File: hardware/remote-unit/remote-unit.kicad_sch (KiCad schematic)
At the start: 54 parts, among them J1 SOL_A, J2 RF Module, J3 ICSP, J4 IO, J5 SOL_B, J6 PWR 12V, J7 UART, J8 I2C, J9 SOLAR, Q1 N >1A@4VGS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

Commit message: Update irrigation controller board
Remove atmega328p
Remove 5v voltage regulator
Replace max485 with max3485
Remove signal relays
Add female headers for ESP32
Add two LEDs
Update BOM based on JLCPCB availability
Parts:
- L1: JLCPCB Part C253606 -> C497847
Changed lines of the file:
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@@
       (effects (font (size 1.27 1.27)) hide)
     )
-    (property "JLCPCB Part" "C253606" (at 184.15 24.13 0)
+    (property "JLCPCB Part" "C497847" (at 184.15 24.13 0)
       (effects (font (size 1.27 1.27)) hide)
     )

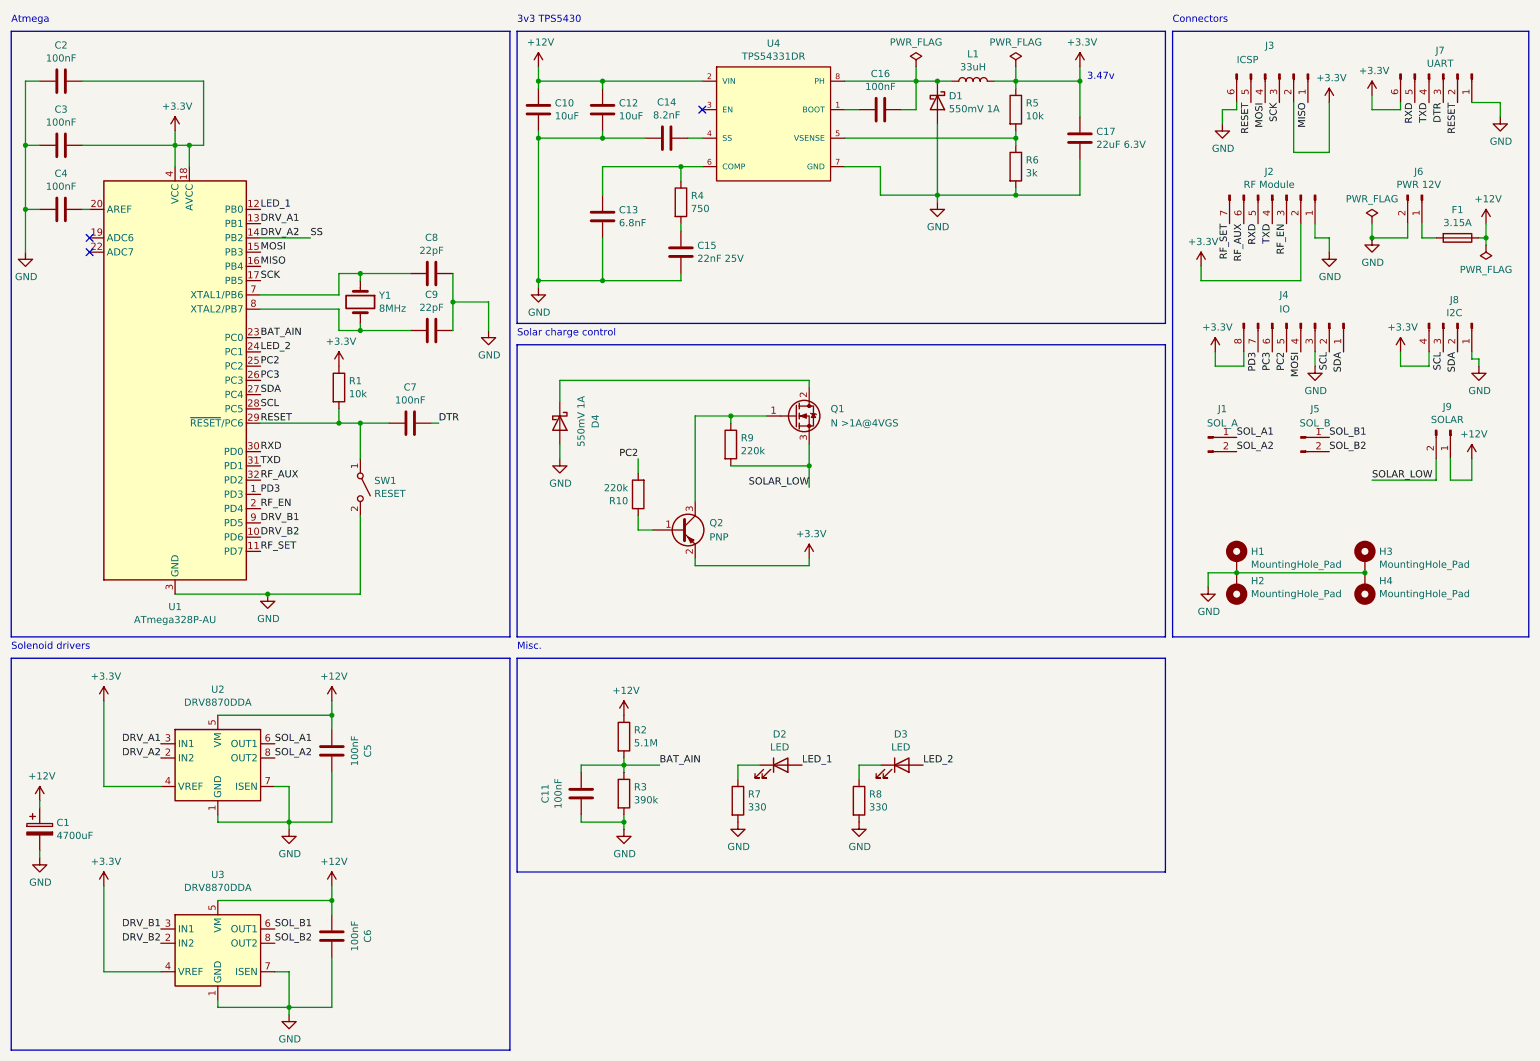
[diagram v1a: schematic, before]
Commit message: Add RS485 to remote unit schematic
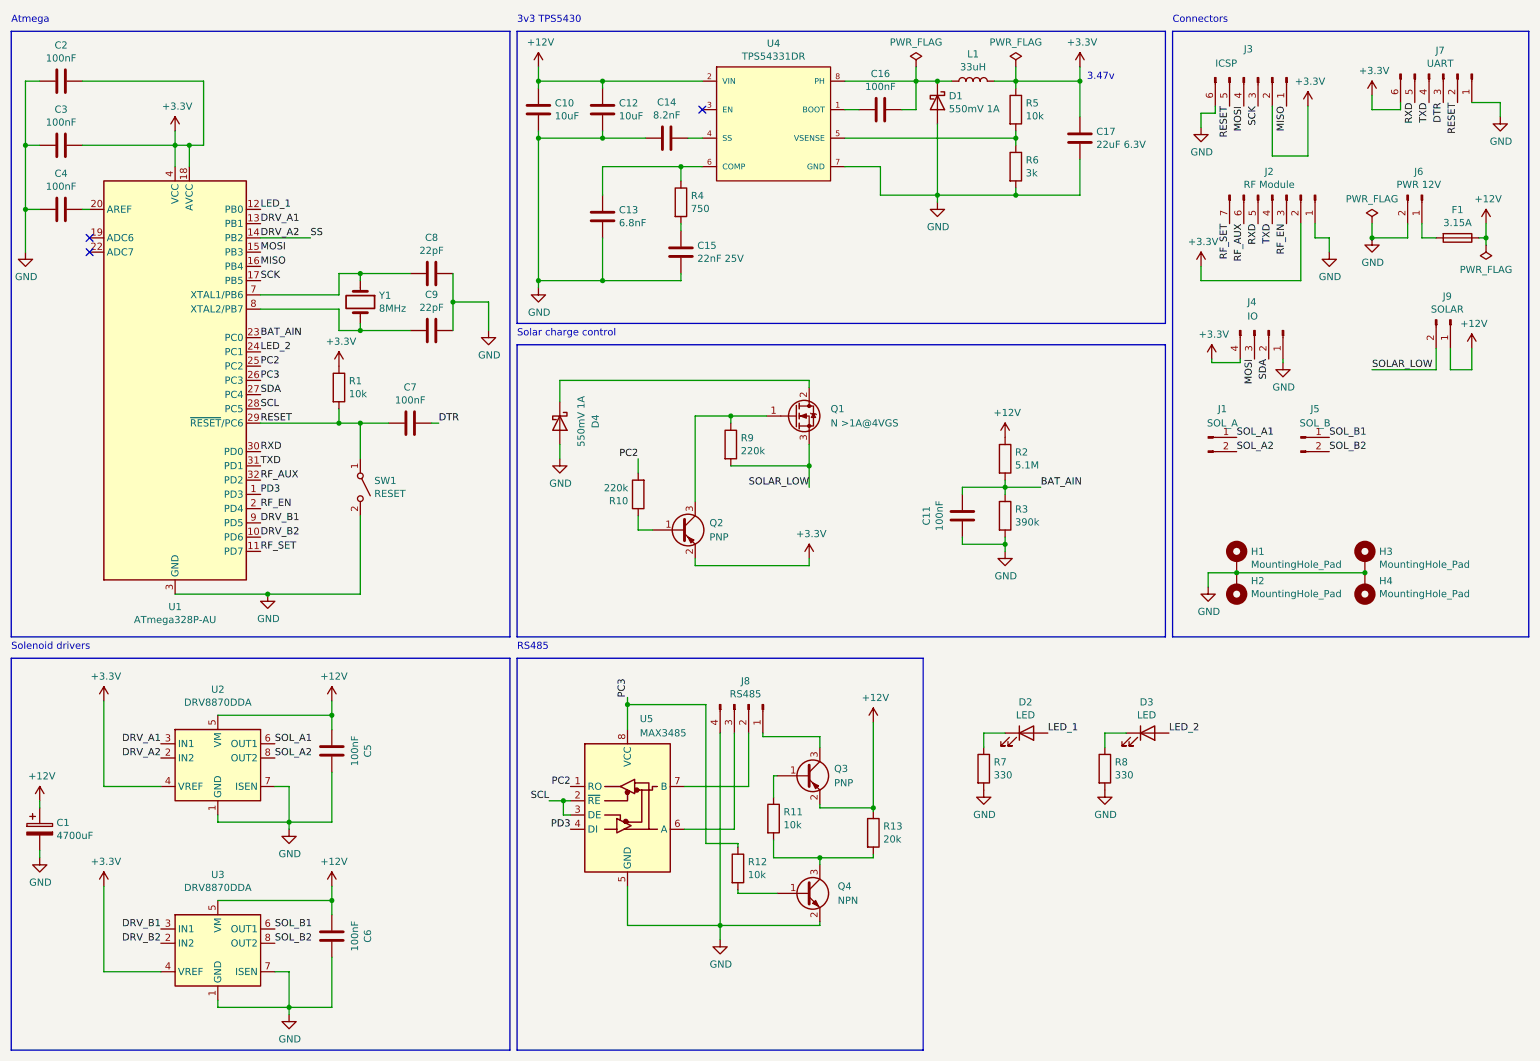
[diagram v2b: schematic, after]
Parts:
- added Q3: PNP, Package_TO_SOT_SMD:SOT-23, symbol Device:Q_PNP_BEC
- added Q4: NPN, Package_TO_SOT_SMD:SOT-23, symbol Device:Q_NPN_BEC
- added R11, R12: 10k, Resistor_SMD:R_0402_1005Metric, symbol Device:R
- added R13: 20k, Resistor_SMD:R_0402_1005Metric, symbol Device:R
- added U5: MAX3485, Package_DIP:DIP-8_W7.62mm, symbol Interface_UART:MAX3485
- C1: symbol remote-unit-rescue:CP-Device -> Device:C_Polarized
- J1, J5, J6, J9: symbol remote-unit-rescue:Conn_01x02_Male-Connector -> Connector:Conn_01x02_Pin
- J2: symbol remote-unit-rescue:Conn_01x07_Male-Connector -> Connector:Conn_01x07_Pin
- J3, J7: symbol remote-unit-rescue:Conn_01x06_Male-Connector -> Connector:Conn_01x06_Pin
- J4: symbol remote-unit-rescue:Conn_01x08_Male-Connector -> Connector:Conn_01x04_Pin
- J8: value I2C -> RS485
- U1: symbol remote-unit-rescue:ATmega328P-AU-MCU_Microchip_ATmega -> MCU_Microchip_ATmega:ATmega328P-A
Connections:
- net +12V: now also Q3.2 (E), R13.1
- net +3.3V: now also J4.4 (Pin_4); no longer J4.8 (Pin_8), J8.4 (Pin_4)
- net GND: now also J4.1 (Pin_1), J8.4 (Pin_4), Q4.2 (E), U5.5 (GND); no longer J4.3 (Pin_3), J8.1 (Pin_1)
- net MOSI: now also J4.3 (Pin_3); no longer J4.4 (Pin_4)
- net PC2: now also U5.1 (RO); no longer J4.5 (Pin_5)
- net PC3: now also R12.1, U5.8 (VCC); no longer J4.6 (Pin_6)
- net PD3: now also U5.4 (DI); no longer J4.7 (Pin_7)
- net SCL: now also U5.2 (~{RE}), U5.3 (DE); no longer J4.2 (Pin_2), J8.3 (Pin_3)
- net SDA: now also J4.2 (Pin_2); no longer J4.1 (Pin_1), J8.2 (Pin_2)
- new net: J8.1 (Pin_1), Q3.3 (C)
- new net: J8.2 (Pin_2), U5.7 (B)
- new net: J8.3 (Pin_3), U5.6 (A)
- new net: Q4.1 (B), R12.2
- new net: Q4.3 (C), R11.2, R13.2
- new net: Q3.1 (B), R11.1
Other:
- note added: "RS485"
- note removed: "Misc."
- moved on the sheet: C11, D2, D3, J3, J8, J9, R2, R3, R7, R8

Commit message: Update remote unit PCB
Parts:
- removed J4: IO, Connector_PinHeader_2.54mm:PinHeader_2x04_P2.54mm_Vertical, symbol Connector:Conn_01x04_Pin
- D2, D3: footprint LED_SMD:LED_0603_1608Metric_Castellated -> LED_SMD:LED_0603_1608Metric
- H1, H2, H3, H4: now left out of the parts list
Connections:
- net PC2: no longer R10.2
- net SCL renamed PC5
- net SDA renamed PC4
- net PC4: now also R10.2
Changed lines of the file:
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@@
-    (stroke (width 0) (type default))
-  )
-  (wire (pts (xy 239.395 73.66) (xy 239.395 74.295))
     (stroke (width 0) (type default))
   )
@@
     (stroke (width 0) (type default))
   )
-  (wire (pts (xy 231.775 73.66) (xy 231.775 74.295))
-    (stroke (width 0) (type default))
-  )
   (wire (pts (xy 243.84 37.465) (xy 243.84 28.575))
     (stroke (width 0) (type default))
@@
     (stroke (width 0) (type default))
   )
-  (wire (pts (xy 226.695 74.295) (xy 226.695 73.66))
-    (stroke (width 0) (type default))
-  )
   (wire (pts (xy 189.865 96.52) (xy 189.865 97.79))
     (stroke (width 0) (type default))
@@
     (stroke (width 0) (type default))
   )
-  (wire (pts (xy 231.775 74.295) (xy 226.695 74.295))
-    (stroke (width 0) (type default))
-  )
   (wire (pts (xy 154.94 77.47) (xy 154.94 78.74))
     (stroke (width 0) (type default))
@@
   (label "LED_2" (at 57.15 72.39 0) (fields_autoplaced)
     (effects (font (size 1.27 1.27)) (justify left bottom))
-  )
-  (label "MOSI" (at 234.315 73.66 270) (fields_autoplaced)
-    (effects (font (size 1.27 1.27)) (justify right bottom))
   )
   (label "RXD" (at 234.95 49.53 270) (fields_autoplaced)
@@
     (effects (font (size 1.27 1.27)) (justify left bottom))
   )
-  (label "SDA" (at 57.15 80.01 0) (fields_autoplaced)
+  (label "PC4" (at 57.15 80.01 0) (fields_autoplaced)
     (effects (font (size 1.27 1.27)) (justify left bottom))
   )
@@
     (effects (font (size 1.27 1.27)) (justify left bottom))
   )
-  (label "SCL" (at 108.585 152.4 180) (fields_autoplaced)
+  (label "PC5" (at 108.585 152.4 180) (fields_autoplaced)
     (effects (font (size 1.27 1.27)) (justify right bottom))
   )
@@
     (effects (font (size 1.27 1.27)) (justify right bottom))
   )
-  (label "SDA" (at 236.855 73.66 270) (fields_autoplaced)
-    (effects (font (size 1.27 1.27)) (justify right bottom))
-  )
   (label "MISO" (at 240.03 28.575 270) (fields_autoplaced)
     (effects (font (size 1.27 1.27)) (justify right bottom))
@@
     (effects (font (size 1.27 1.27)) (justify left bottom))
   )
-  (label "PC2" (at 124.46 91.44 180) (fields_autoplaced)
+  (label "PC4" (at 124.46 91.44 180) (fields_autoplaced)
     (effects (font (size 1.27 1.27)) (justify right bottom))
   )
@@
     (effects (font (size 1.27 1.27)) (justify left bottom))
   )
-  (label "SCL" (at 57.15 82.55 0) (fields_autoplaced)
+  (label "PC5" (at 57.15 82.55 0) (fields_autoplaced)
     (effects (font (size 1.27 1.27)) (justify left bottom))
   )
@@
       (effects (font (size 1.27 1.27)))
     )
-    (property "Footprint" "LED_SMD:LED_0603_1608Metric_Castellated" (at 193.675 140.335 0)
+    (property "Footprint" "LED_SMD:LED_0603_1608Metric" (at 193.675 140.335 0)
       (effects (font (size 1.27 1.27)) hide)
     )
@@
       (effects (font (size 1.27 1.27)))
     )
-    (property "Footprint" "LED_SMD:LED_0603_1608Metric_Castellated" (at 215.265 140.335 0)
+    (property "Footprint" "LED_SMD:LED_0603_1608Metric" (at 215.265 140.335 0)
       (effects (font (size 1.27 1.27)) hide)
     )
@@
     )
   )
-  (symbol (lib_id "Connector:Conn_01x04_Pin") (at 236.855 68.58 270) (unit 1)
-    (in_bom yes) (on_board yes) (dnp no)
-    (property "Reference" "J4" (at 233.045 63.5 90)
-      (effects (font (size 1.27 1.27)) (justify left))
-    )
-    (property "Value" "IO" (at 233.045 66.04 90)
-      (effects (font (size 1.27 1.27)) (justify left))
-    )
-    (property "Footprint" "Connector_PinHeader_2.54mm:PinHeader_2x04_P2.54mm_Vertical" (at 236.855 68.58 0)
-      (effects (font (size 1.27 1.27)) hide)
-    )
-    (property "Datasheet" "~" (at 236.855 68.58 0)
-      (effects (font (size 1.27 1.27)) hide)
-    )
-    (property "Purchase Link" "https://au.element14.com/amphenol-icc/77313-801-20lf/conn-header-20pos-2row-2-54mm/dp/3728842" (at 236.855 68.58 0)
-      (effects (font (size 1.27 1.27)) hide)
-    )
-    (pin "1")
-    (pin "2")
-    (pin "3")
-    (pin "4")
-    (instances
-      (project "remote-unit"
-        (path "/18be3b1b-9bcf-4c4f-bb2a-ca2504ea30e0"
-          (reference "J4") (unit 1)
-        )
-      )
-    )
-  )
-  (symbol (lib_id "power:+3.3V") (at 226.695 73.66 0) (unit 1)
-    (in_bom yes) (on_board yes) (dnp no)
-    (property "Reference" "#PWR022" (at 226.695 77.47 0)
-      (effects (font (size 1.27 1.27)) hide)
-    )
-    (property "Value" "+3.3V" (at 227.076 69.2658 0)
-      (effects (font (size 1.27 1.27)))
-    )
-    (property "Footprint" "" (at 226.695 73.66 0)
-      (effects (font (size 1.27 1.27)) hide)
-    )
-    (property "Datasheet" "" (at 226.695 73.66 0)
-      (effects (font (size 1.27 1.27)) hide)
-    )
-    (pin "1")
-    (instances
-      (project "remote-unit"
-        (path "/18be3b1b-9bcf-4c4f-bb2a-ca2504ea30e0"
-          (reference "#PWR022") (unit 1)
-        )
-      )
-    )
-  )
-  (symbol (lib_id "power:GND") (at 239.395 74.295 0) (unit 1)
-    (in_bom yes) (on_board yes) (dnp no)
-    (property "Reference" "#PWR026" (at 239.395 80.645 0)
-      (effects (font (size 1.27 1.27)) hide)
-    )
-    (property "Value" "GND" (at 239.522 78.6892 0)
-      (effects (font (size 1.27 1.27)))
-    )
-    (property "Footprint" "" (at 239.395 74.295 0)
-      (effects (font (size 1.27 1.27)) hide)
-    )
-    (property "Datasheet" "" (at 239.395 74.295 0)
-      (effects (font (size 1.27 1.27)) hide)
-    )
-    (pin "1")
-    (instances
-      (project "remote-unit"
-        (path "/18be3b1b-9bcf-4c4f-bb2a-ca2504ea30e0"
-          (reference "#PWR026") (unit 1)
-        )
-      )
-    )
-  )
   (symbol (lib_id "power:+3.3V") (at 29.21 134.62 0) (unit 1)
     (in_bom yes) (on_board yes) (dnp no)
@@
   )
   (symbol (lib_id "Mechanical:MountingHole_Pad") (at 231.14 109.22 0) (unit 1)
-    (in_bom yes) (on_board yes) (dnp no)
+    (in_bom no) (on_board yes) (dnp no)
     (property "Reference" "H1" (at 233.68 107.9754 0)
       (effects (font (size 1.27 1.27)) (justify left))
@@
   )
   (symbol (lib_id "Mechanical:MountingHole_Pad") (at 254 109.22 0) (unit 1)
-    (in_bom yes) (on_board yes) (dnp no)
+    (in_bom no) (on_board yes) (dnp no)
     (property "Reference" "H3" (at 256.54 107.9754 0)
       (effects (font (size 1.27 1.27)) (justify left))
@@
   )
   (symbol (lib_id "Mechanical:MountingHole_Pad") (at 231.14 114.3 180) (unit 1)
-    (in_bom yes) (on_board yes) (dnp no)
+    (in_bom no) (on_board yes) (dnp no)
     (property "Reference" "H2" (at 233.68 113.2078 0)
       (effects (font (size 1.27 1.27)) (justify right))
@@
   )
   (symbol (lib_id "Mechanical:MountingHole_Pad") (at 254 114.3 180) (unit 1)
-    (in_bom yes) (on_board yes) (dnp no)
+    (in_bom no) (on_board yes) (dnp no)
     (property "Reference" "H4" (at 256.54 113.2078 0)
       (effects (font (size 1.27 1.27)) (justify right))

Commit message: Fix remote unit charge control FET pin mismatch
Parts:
- Q1: footprint Package_TO_SOT_SMD:SOT-23-3 -> Package_TO_SOT_SMD:SOT-23; symbol Transistor_FET:IRLIZ44N -> Transistor_FET:IRLML0030
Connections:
- net SOLAR_LOW: now also Q1.2 (S); no longer Q1.3 (S)
- net at D4.1 (K): now also Q1.3 (D); no longer Q1.2 (D)
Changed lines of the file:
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@@
     )
   )
-  (symbol (lib_id "Transistor_FET:IRLIZ44N") (at 152.4 83.82 0) (unit 1)
+  (symbol (lib_id "Transistor_FET:IRLML0030") (at 152.4 83.82 0) (unit 1)
     (in_bom yes) (on_board yes) (dnp no) (fields_autoplaced)
     (property "Reference" "Q1" (at 158.75 82.55 0)
@@
       (effects (font (size 1.27 1.27)) (justify left))
     )
-    (property "Footprint" "Package_TO_SOT_SMD:SOT-23-3" (at 158.75 85.725 0)
+    (property "Footprint" "Package_TO_SOT_SMD:SOT-23" (at 157.48 85.725 0)
       (effects (font (size 1.27 1.27) italic) (justify left) hide)
     )
-    (property "Datasheet" "http://www.irf.com/product-info/datasheets/data/irliz44n.pdf" (at 152.4 83.82 0)
+    (property "Datasheet" "https://www.infineon.com/dgdl/irlml0030pbf.pdf?fileId=5546d462533600a401535664773825df" (at 152.4 83.82 0)
       (effects (font (size 1.27 1.27)) (justify left) hide)
     )

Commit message: Remote unit Kicad upgrade
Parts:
- J1, J2, J3, J5, J6, J7, J9, SW1: now left out of the parts list

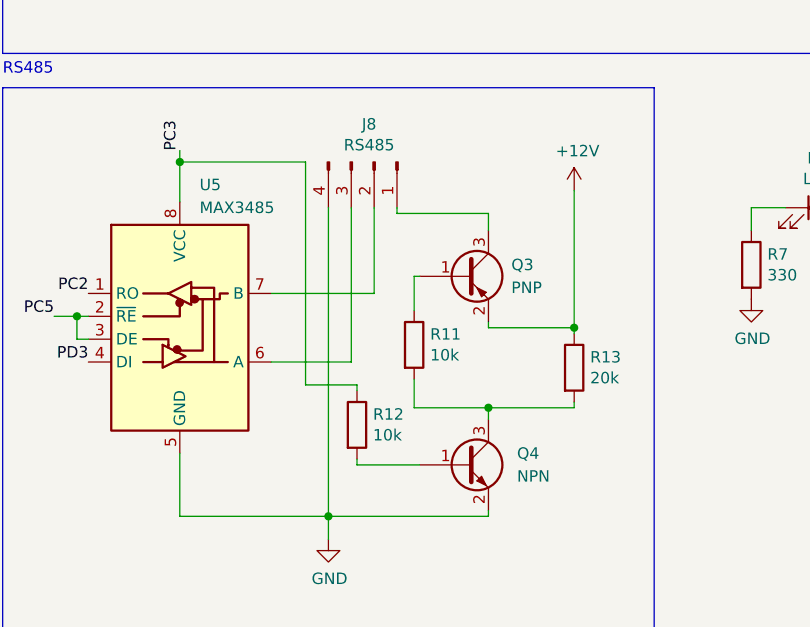
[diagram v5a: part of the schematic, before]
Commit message: Fix remote unit rs485 sensor power supply circuit
Replace BJT with mosfet with appropriate source-gate voltage rating
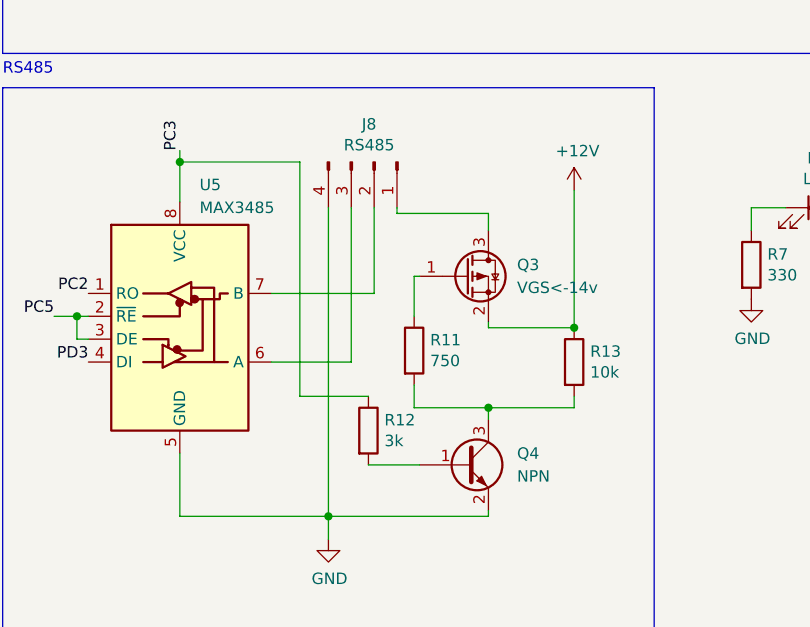
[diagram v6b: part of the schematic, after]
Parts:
- Q3: value PNP -> VGS<-14v; symbol Device:Q_PNP_BEC -> Transistor_FET:Q_PMOS_GSD; JLCPCB Part C8542 -> C8492; Purchase Link NA -> (none)
- R11: value 10k -> 750; footprint Resistor_SMD:R_0402_1005Metric -> Resistor_SMD:R_0603_1608Metric; JLCPCB Part C25744 -> C23241
- R12: value 10k -> 3k; footprint Resistor_SMD:R_0402_1005Metric -> Resistor_SMD:R_0603_1608Metric; JLCPCB Part C25744 -> C4211
- R13: value 20k -> 10k; JLCPCB Part C25765 -> C25744
